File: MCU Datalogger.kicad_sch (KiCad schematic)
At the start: 25 parts, among them U1 24LC1025, U2 DS1337S+, U3 24LC1025, U4 ATMEGA328-AU, Y1 32.768 KHz, Y2 16 MHz

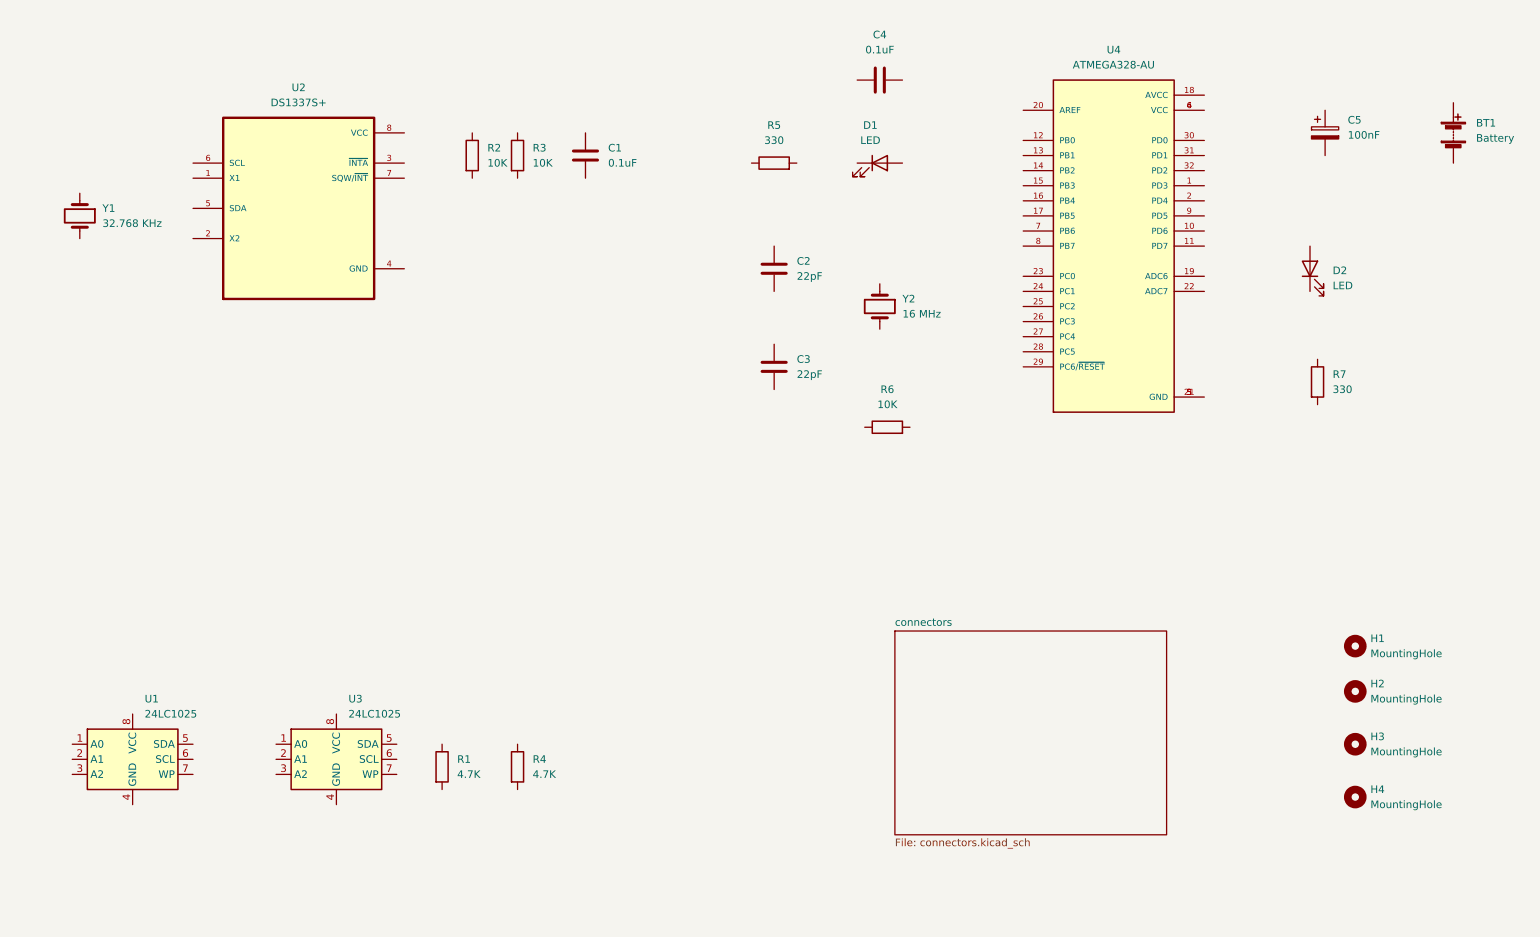
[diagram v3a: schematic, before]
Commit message: Completed the wiring of main sheet.
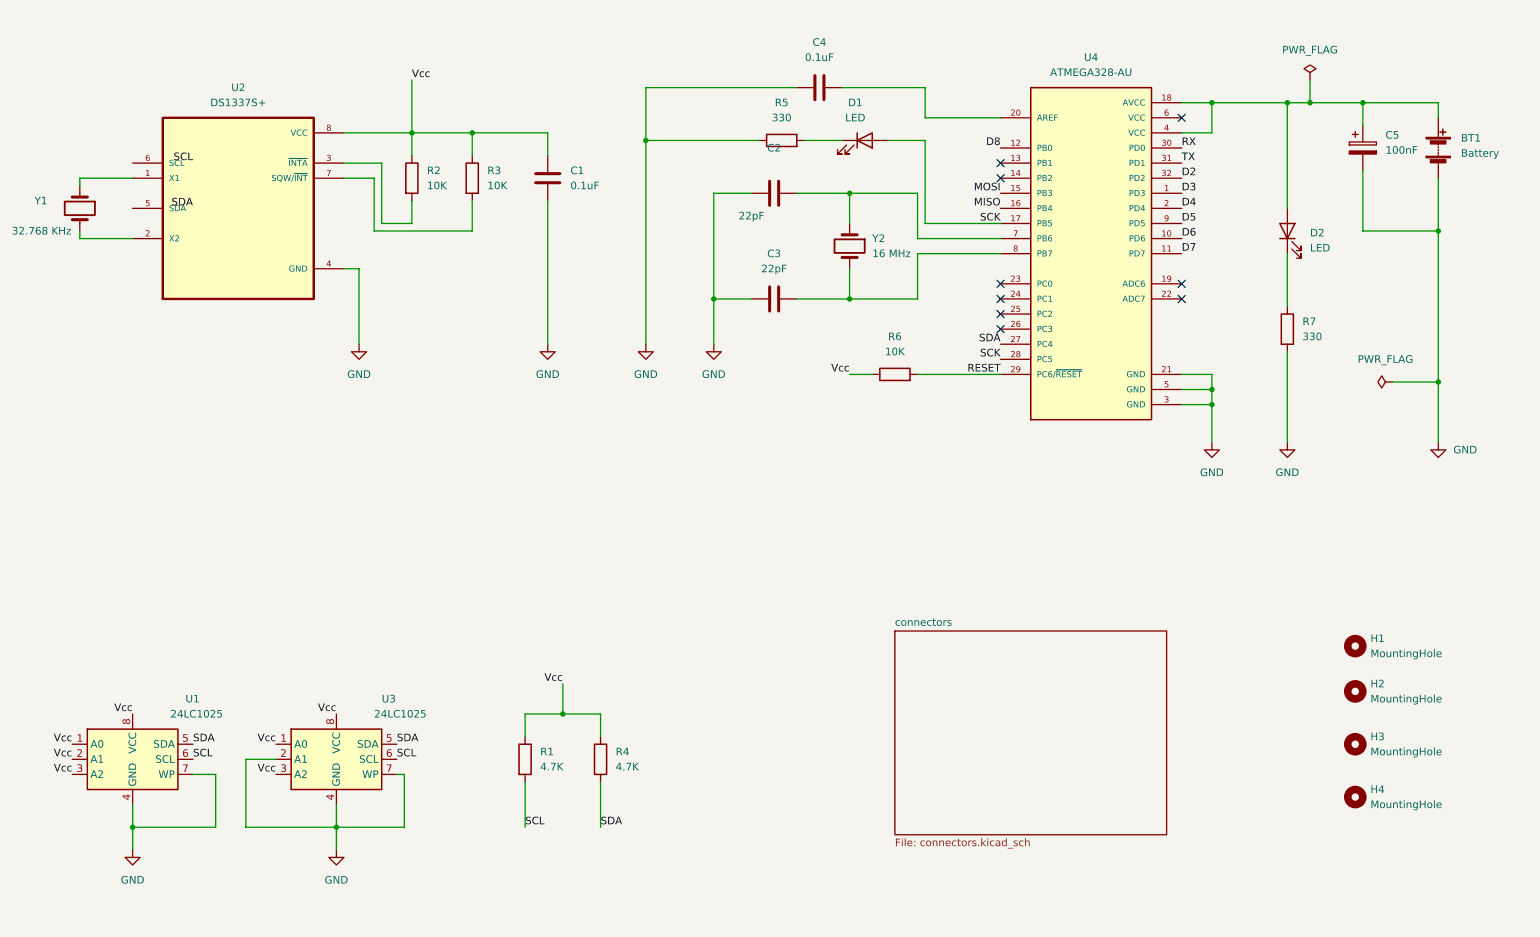
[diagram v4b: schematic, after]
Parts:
- U4: footprint Footprints:QFP80P900X900X120-32N -> QFP80P900X900X120-32N
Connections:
- net at BT1.1 (+): now also C5.1, D2.2 (A), U4.18 (AVCC), U4.4 (VCC)
- net GND: now reaches BT1.2 (-)
- net GND: now also C1.2, C2.1, C3.1, C4.1, C5.2, R5.1, R7.2, U1.4 (GND), U1.7 (WP), U2.4 (GND), U3.2 (A1), U3.4 (GND), U3.7 (WP), U4.21 (GND), U4.3 (GND), U4.5 (GND)
- net Vcc: now reaches R4.1
- net Vcc: now also C1.1, R1.1, R2.1, R3.1, R6.1, U1.1 (A0), U1.2 (A1), U1.3 (A2), U1.8 (VCC), U2.8 (VCC), U3.1 (A0), U3.3 (A2), U3.8 (VCC)
- net SDA: now reaches R4.2
- net SDA: now also U1.5 (SDA), U3.5 (SDA), U4.27 (PC4)
- net at U2.1 (X1): now also Y1.1
- net at U2.2 (X2): now also Y1.2
- net at U2.3 (~{INTA}): now also R2.2
- net at U2.7 (SQW/~{INT}): now also R3.2
- net SCL: now reaches R1.2
- net SCL: now also U1.6 (SCL), U3.6 (SCL)
- net at C2.2: now also U4.7 (PB6), Y2.1
- net at D2.1 (K): now also R7.1
- net at C4.2: now also U4.20 (AREF)
- net D3: now reaches U4.1 (PD3)
- net D6: now reaches U4.10 (PD6)
- net D7: now reaches U4.11 (PD7)
- net D8: now reaches U4.12 (PB0)
- net MOSI: now reaches U4.15 (PB3)
- net MISO: now reaches U4.16 (PB4)
- net SCK: now reaches U4.17 (PB5)
- net SCK: now also D1.2 (A), U4.28 (PC5)
- net D4: now reaches U4.2 (PD4)
- net RESET: now reaches U4.29 (PC6/~{RESET})
- net RESET: now also R6.2
- net RX: now reaches U4.30 (PD0)
- net TX: now reaches U4.31 (PD1)
- net D2: now reaches U4.32 (PD2)
- net at U4.6 (VCC): no longer U4.4 (VCC)
- net at U4.8 (PB7): now also C3.2, Y2.2
- net D5: now reaches U4.9 (PD5)
- net at D1.1 (K): now also R5.2
- no-connect marks 0 -> 9
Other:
- moved on the sheet: BT1, C1, C2, C3, C4, C5, D1, D2, R1, R2, R3, R4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

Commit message: Completed the wiring of Connectors sheet(2). PS: No ERC error.
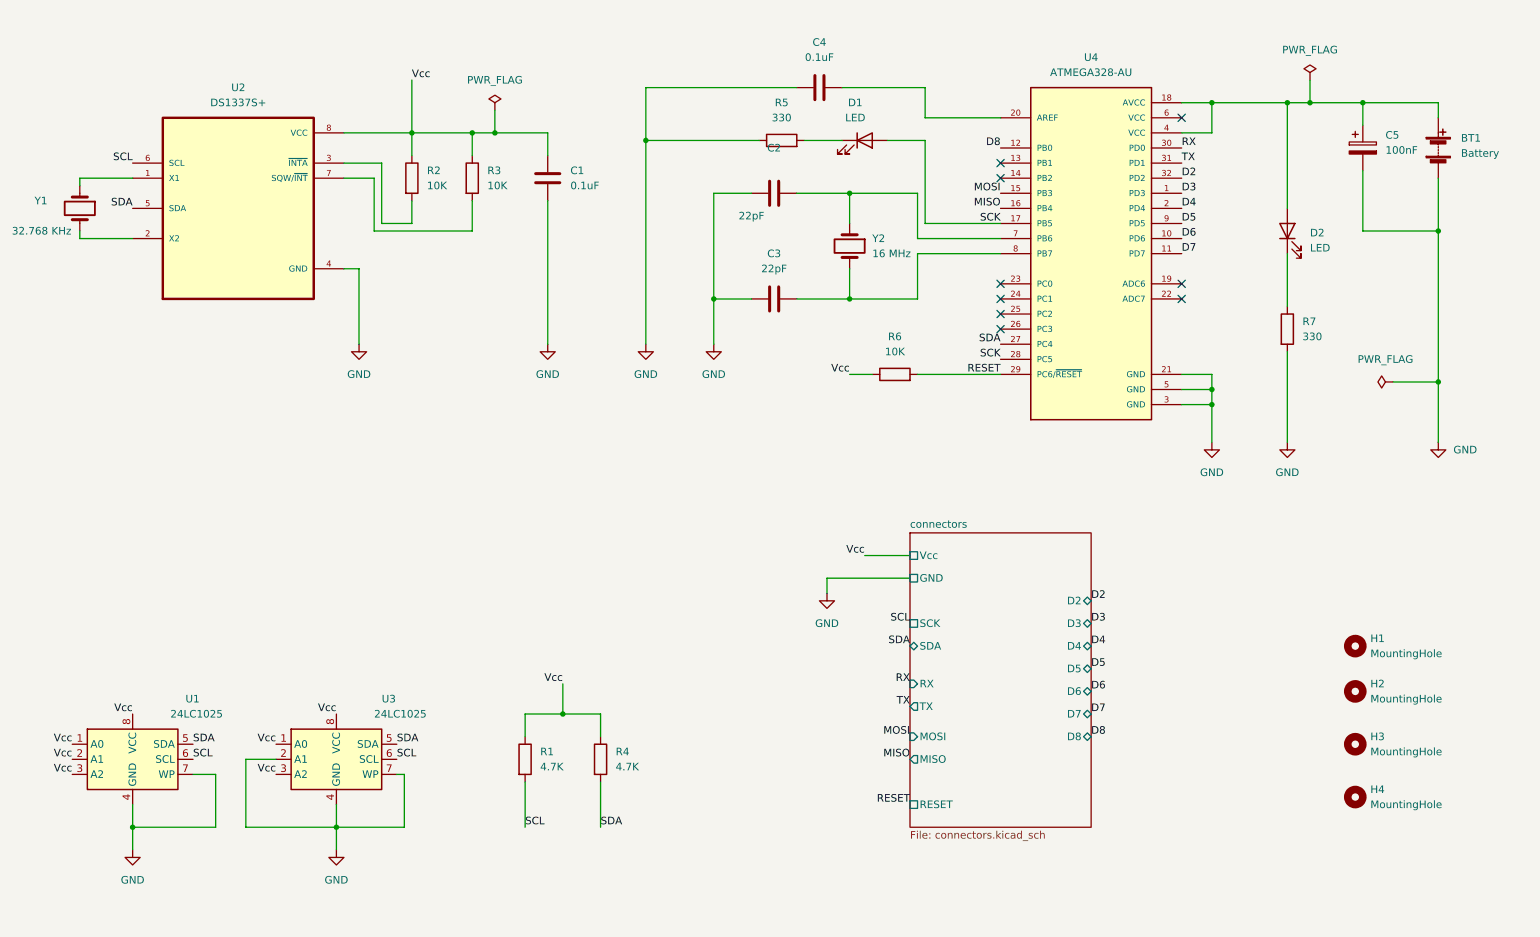
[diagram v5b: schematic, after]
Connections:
- net SCL: now also U2.6 (SCL)
- net SDA: now also U2.5 (SDA)
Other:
- sheet connectors ports: added D2, D3, D4, D5, D6, D7, D8, GND, MISO, MOSI, RESET, RX, SCK, SDA, TX, Vcc; removed none
